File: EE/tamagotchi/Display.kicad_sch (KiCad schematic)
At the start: 0 parts

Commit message: Generic Continutation Checkin
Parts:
- added D1, D10, D11, D12, D2, D3, D4, D5, D6, D7, D8, D9: LED, symbol Device:LED
- added Q1, Q2, Q3, Q4: Q_NMOS_GDS, symbol Transistor_FET:Q_NMOS_GDS
- added R1, R10, R13, R14, R15, R16, R17, R18, R19, R2, R20, R7: R, symbol Device:R
- added R11, R3, R5, R8: 100k, symbol Device:R
- added R12, R4, R6, R9: 33, symbol Device:R
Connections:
- new net: Q3.1 (G), R9.2
- new net: D11.1 (K), D4.1 (K), Q3.2 (D)
- new net: D12.1 (K), D5.1 (K), Q4.2 (D)
- new net: D5.2 (A), R13.2
- new net: D11.2 (A), R19.2
- new net: D10.1 (K), D3.1 (K), Q2.2 (D)
- new net: D3.2 (A), R7.2
- new net: D1.1 (K), D2.1 (K), D6.1 (K), D7.1 (K), D8.1 (K), D9.1 (K), Q1.2 (D)
- new net: D6.2 (A), R14.2
- new net: D9.2 (A), R17.2
- new net: D4.2 (A), R10.2
- new net: D10.2 (A), R18.2
- new net: D12.2 (A), R20.2
- new net: Q4.1 (G), R12.2
- new net: D1.2 (A), R2.2
- new net: D2.2 (A), R1.2
- new net: Q1.1 (G), R4.2
- new net: Q2.1 (G), R6.2
- new net: D7.2 (A), R15.2
- new net: D8.2 (A), R16.2
- new net +3V3: R1.1, R10.1, R13.1, R14.1, R15.1, R16.1, R17.1, R18.1, R19.1, R2.1, R20.1, R7.1
- new net GND: Q1.3 (S), Q2.3 (S), Q3.3 (S), Q4.3 (S), R11.2, R3.2, R5.2, R8.2
- new net GREEN_EN: R11.1, R12.1
- new net RED_EN: R5.1, R6.1
- new net VAPE_EN: R3.1, R4.1
- new net YELLOW_EN: R8.1, R9.1
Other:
- note added: "Alcohol Backlight"
- note added: "Status Indicator"
- note added: "TODO screen"

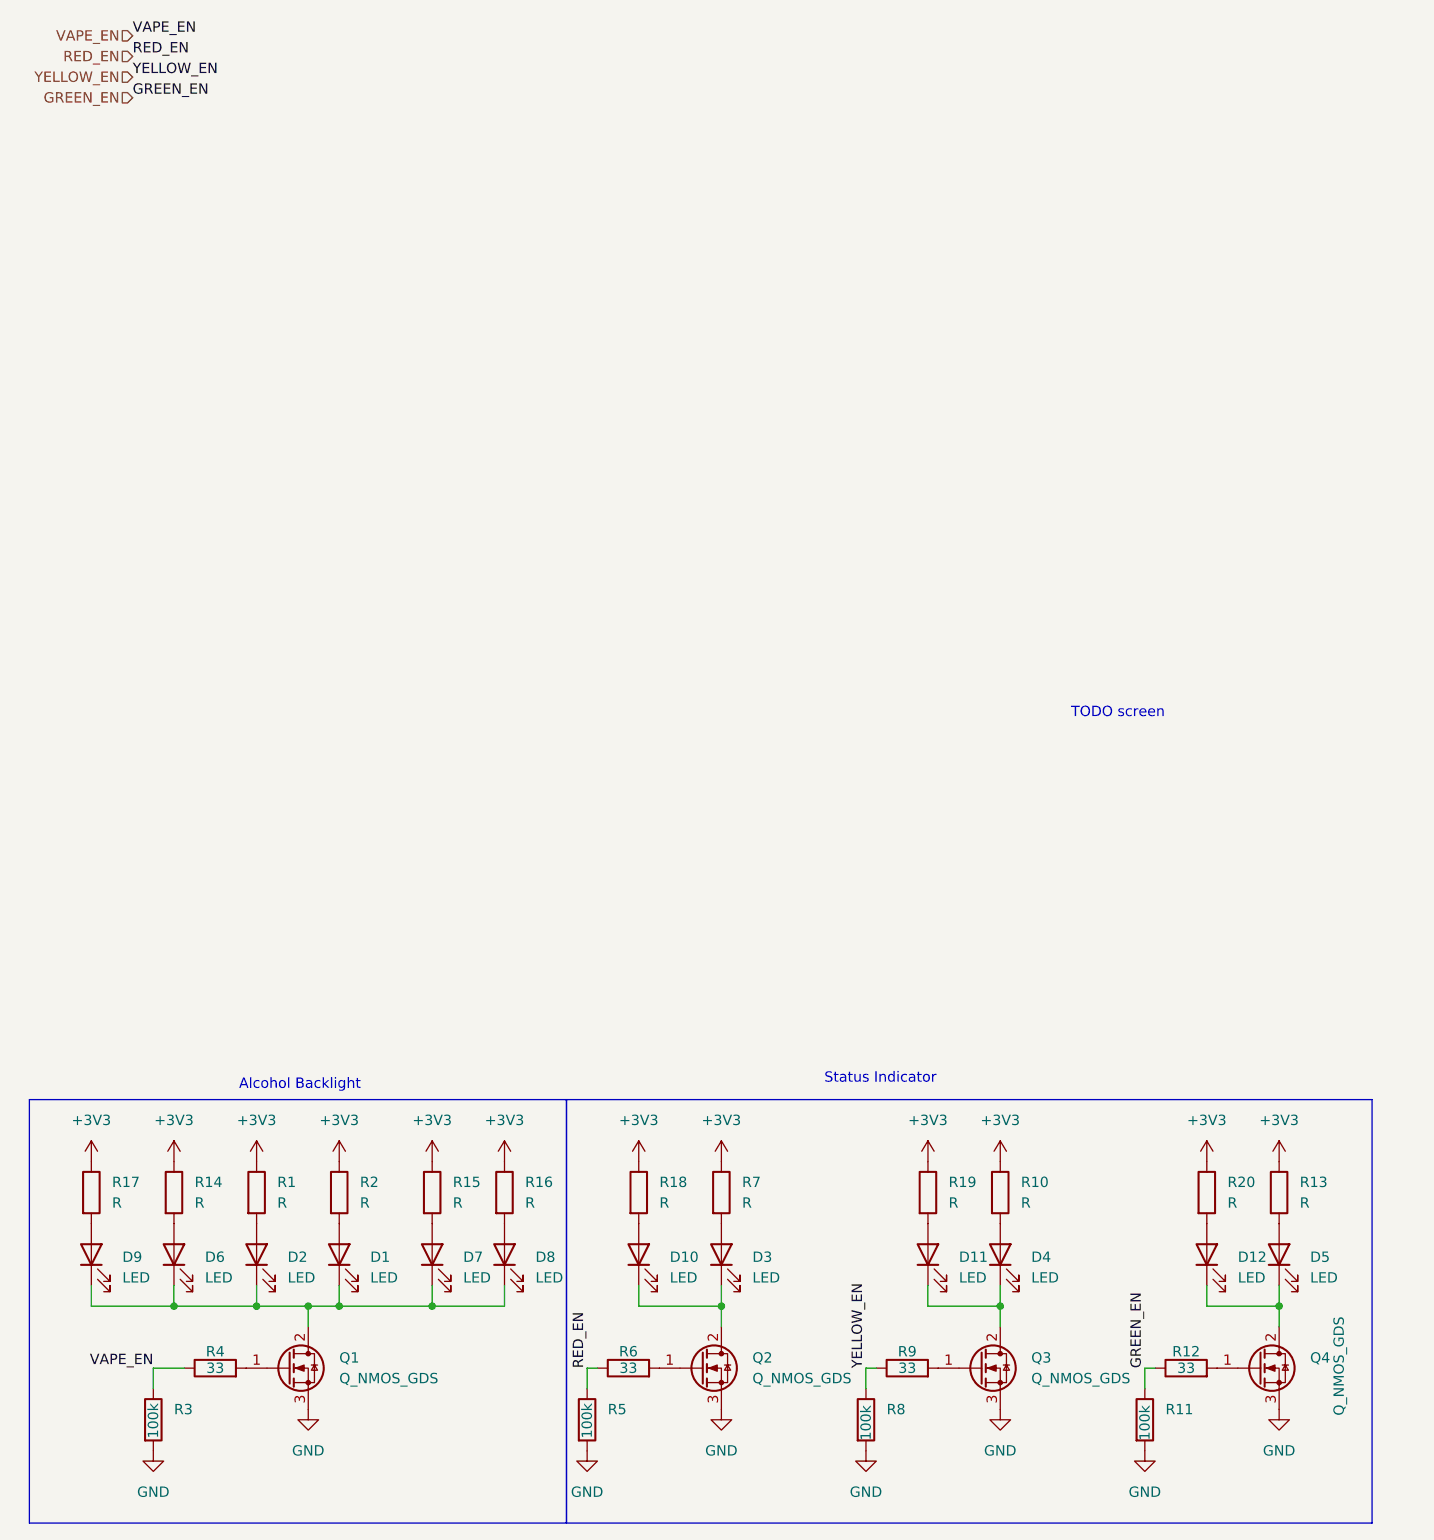
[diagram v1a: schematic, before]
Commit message: WIP - added 3D / footprints for devices. RGY LEDs aren't right
Need to do more outling / ect. super rough placement for everything.
LED footprint for RGY appears just wrong
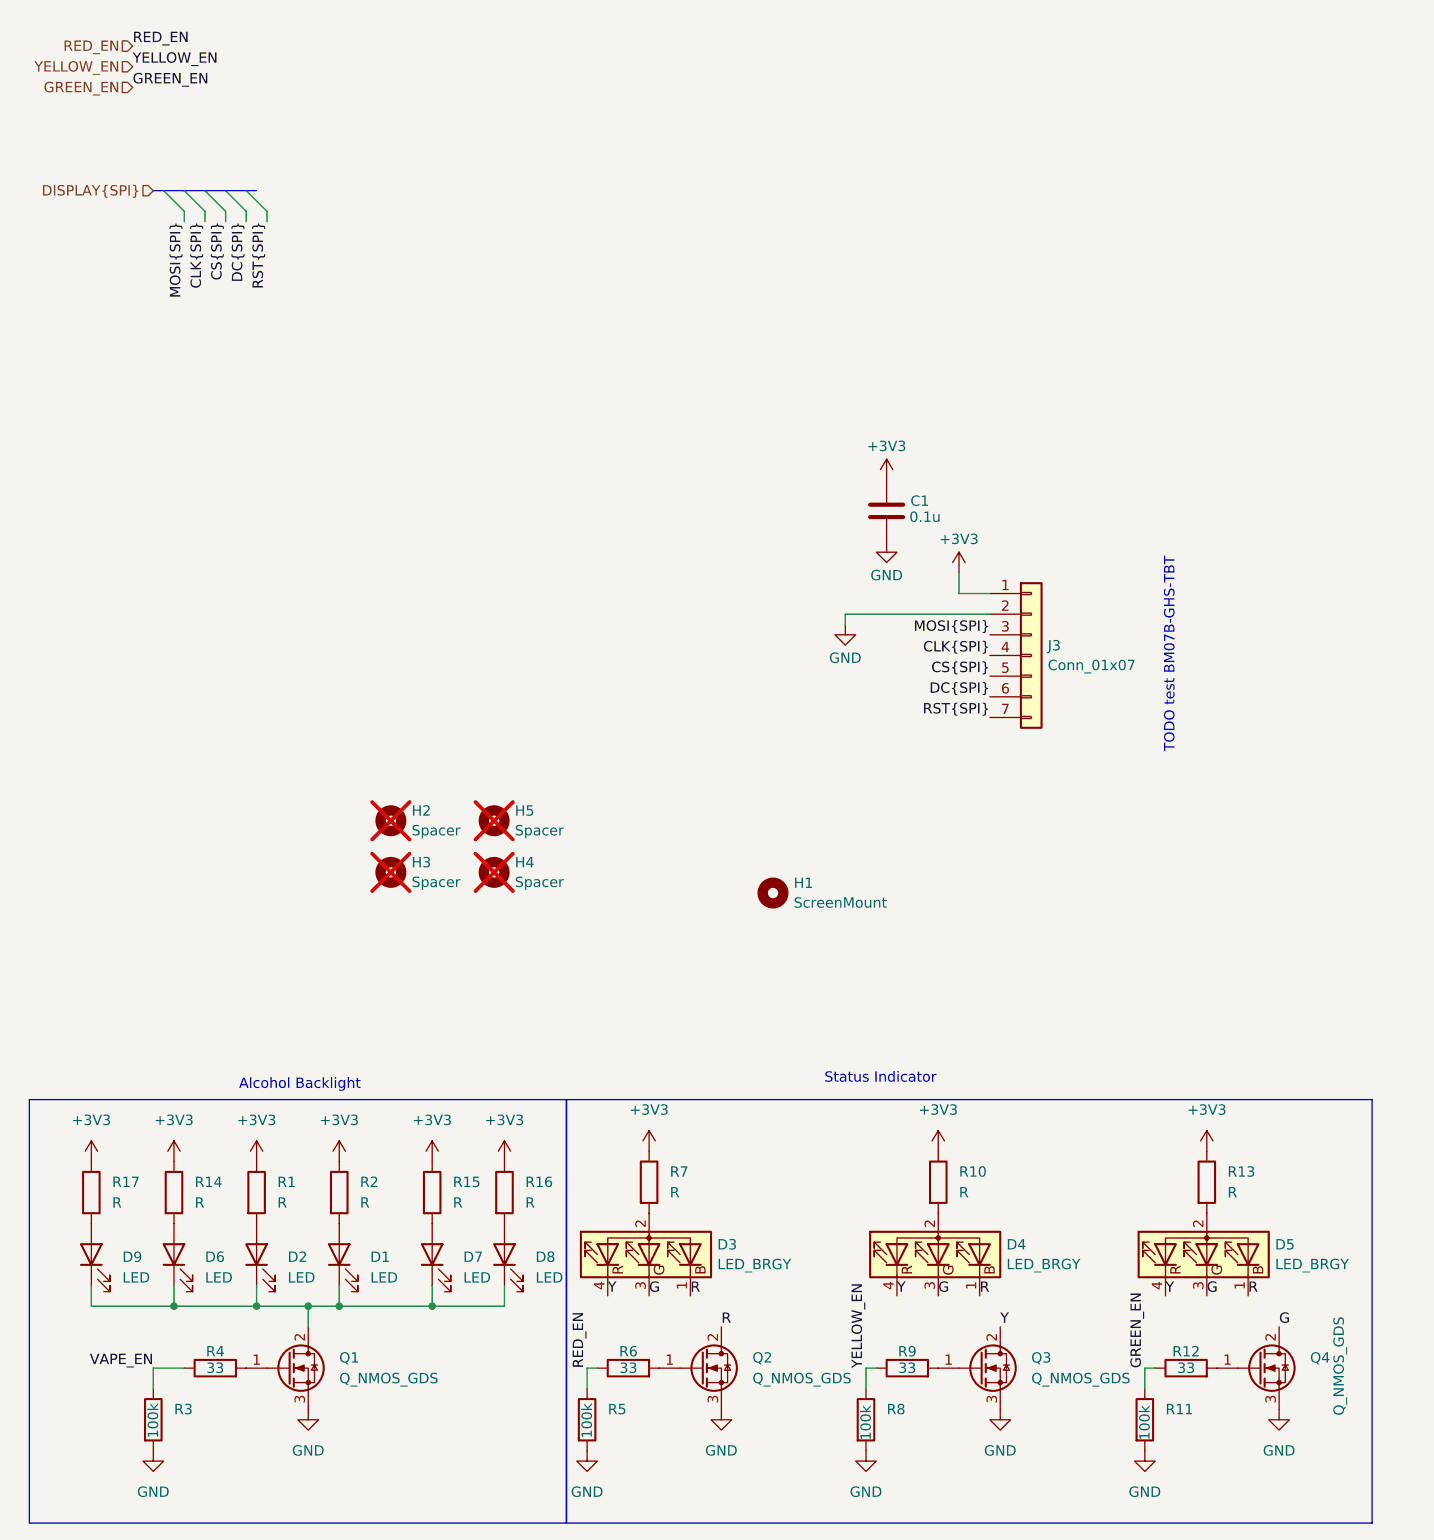
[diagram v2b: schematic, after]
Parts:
- removed D10, D11, D12, D3, D4, D5: LED, symbol Device:LED
- removed R18, R19, R20: R, symbol Device:R
- added C1: 0.1u, Capacitor_SMD:C_0402_1005Metric_Pad0.74x0.62mm_HandSolder, symbol Device:C
- added D3, D4, D5: LED_BRGY, Library:EAST1616RGYA0_EVE, symbol Device:LED_BAGR
- added H1: ScreenMount, Library:ScreenMount, symbol Mechanical:MountingHole
- added H2, H3, H4, H5: Spacer, symbol Mechanical:MountingHole
- added J3: Conn_01x07, symbol Connector_Generic:Conn_01x07
- D1, D2, D6, D7, D8, D9: footprint (none) -> LED_SMD:LED_0603_1608Metric_Pad1.05x0.95mm_HandSolder; MPN (none) -> 150060BS55040
- R1, R10, R11, R12, R13, R14, R15, R16, R17, R2, R3, R4, R5, R6, R7, R8, R9: footprint (none) -> Resistor_SMD:R_0402_1005Metric_Pad0.72x0.64mm_HandSolder
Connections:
- net +3V3: now also C1.1, J3.1 (Pin_1)
- net GND: now also C1.2, J3.2 (Pin_2)
- net Y: now reaches Q3.2 (D)
- net Y: now also D3.4 (RK), D4.4 (RK), D5.4 (RK)
- net G: now reaches Q4.2 (D)
- net G: now also D3.3 (GK), D4.3 (GK), D5.3 (GK)
- net at R13.2: now also D5.2 (A)
- net R: now reaches Q2.2 (D)
- net R: now also D3.1 (BK), D4.1 (BK), D5.1 (BK)
- net at R7.2: now also D3.2 (A)
- net at R10.2: now also D4.2 (A)
- new net CLK{SPI}: J3.4 (Pin_4)
- new net CS{SPI}: J3.5 (Pin_5)
- new net DC{SPI}: J3.6 (Pin_6)
- new net MOSI{SPI}: J3.3 (Pin_3)
- new net RST{SPI}: J3.7 (Pin_7)
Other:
- note added: "TODO test BM07B-GHS-TBT"
- note removed: "TODO screen"

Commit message: Footprints and mechanical parts assigned
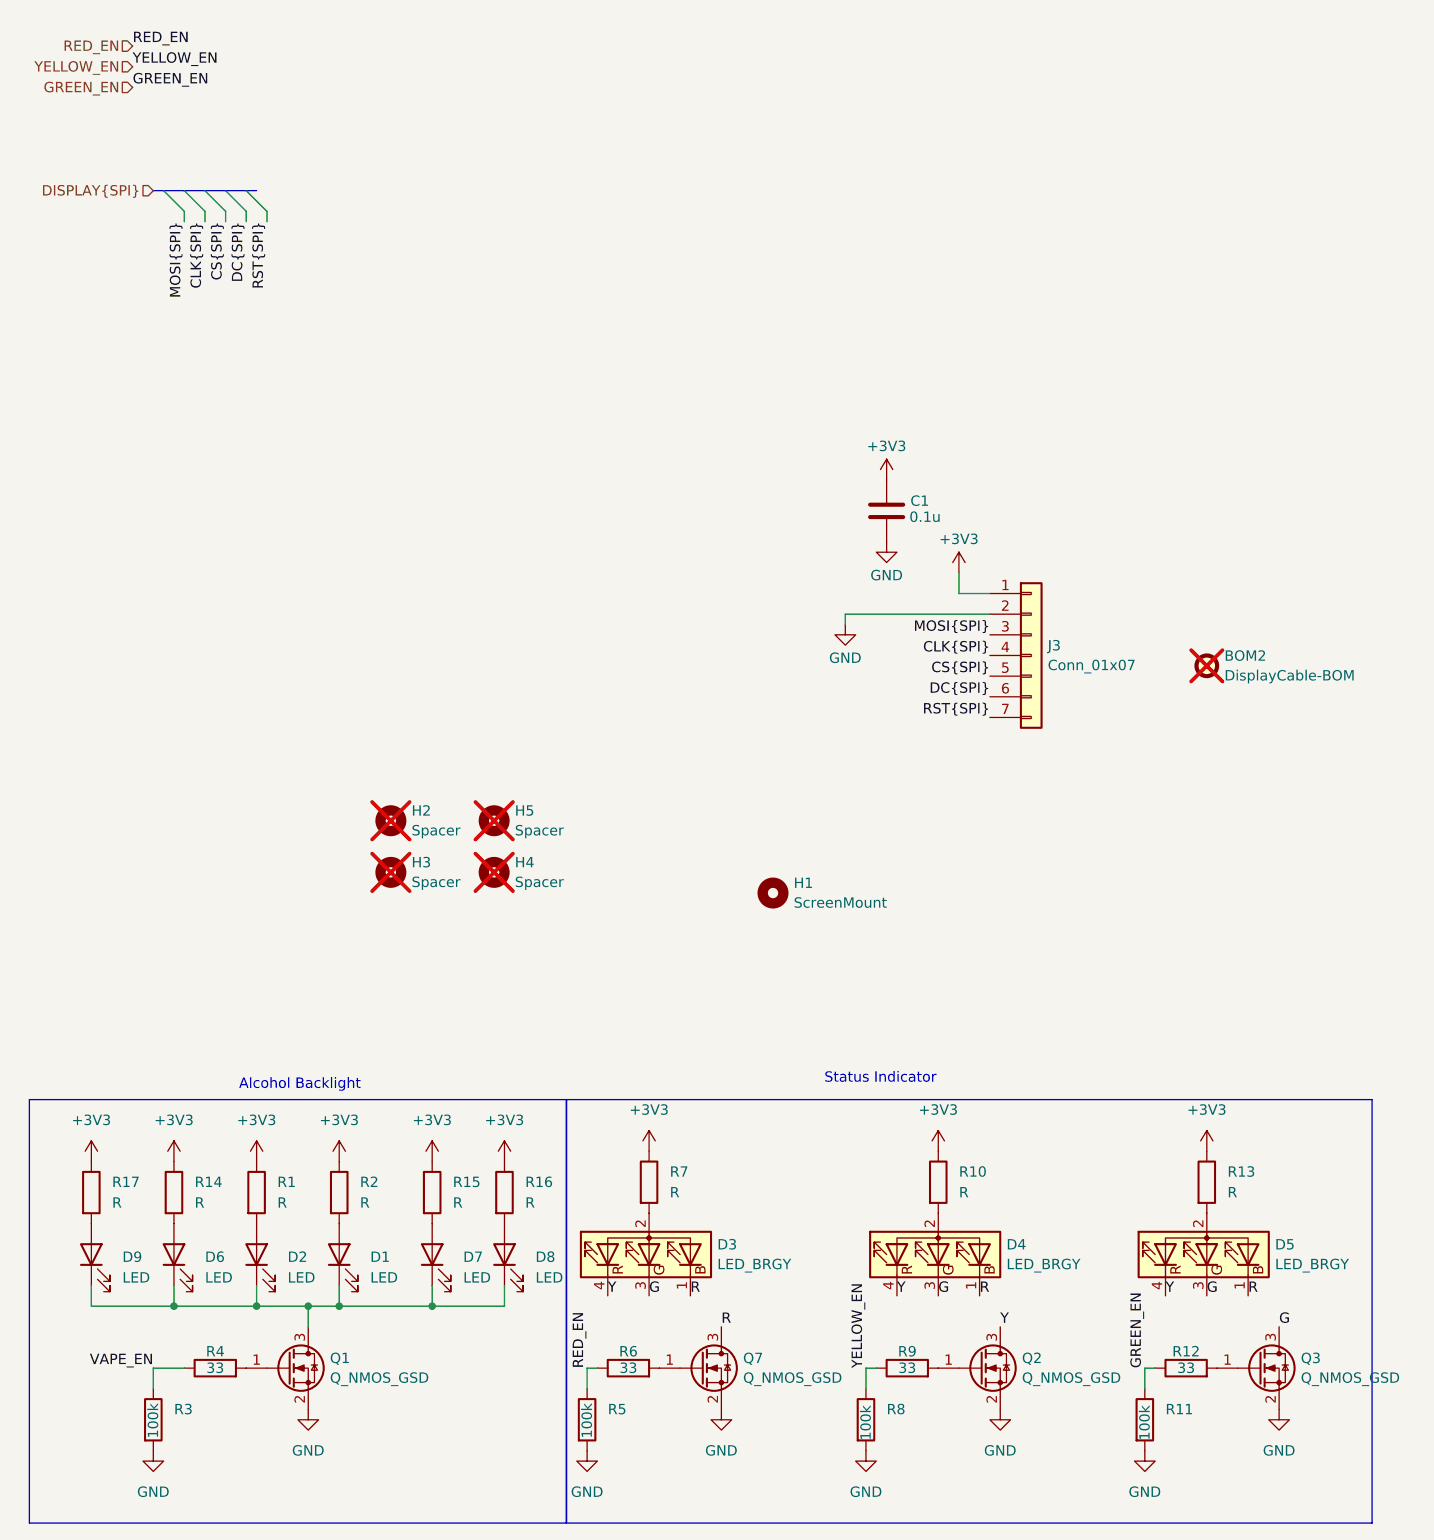
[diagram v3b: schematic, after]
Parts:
- removed Q1, Q2, Q3, Q4: Q_NMOS_GDS, symbol Transistor_FET:Q_NMOS_GDS
- added BOM2: DisplayCable-BOM, symbol Mechanical:Fiducial
- added Q1, Q2, Q3, Q7: Q_NMOS_GSD, Package_TO_SOT_SMD:SOT-23, symbol Transistor_FET:Q_NMOS_GSD
- J3: footprint (none) -> Library:MOLEX_532610771; MPN (none) -> 0532610771; TODO BM07B-GHS-TBT -> (none)
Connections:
- net G: now also Q3.3 (D)
- net GND: now also Q1.2 (S), Q2.2 (S), Q3.2 (S), Q7.2 (S)
- net R: now also Q7.3 (D)
- net Y: now also Q2.3 (D)
- net at R9.2: now also Q2.1 (G)
- net at D1.1 (K), D2.1 (K), D6.1 (K)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: now also Q1.3 (D)
- net at R12.2: now also Q3.1 (G)
- net at R4.2: now also Q1.1 (G)
- net at R6.2: now also Q7.1 (G)
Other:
- note removed: "TODO test BM07B-GHS-TBT"

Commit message: Migrated to 4 Layer. Added 3v3 and gnd layers
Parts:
- removed D2: LED, LED_SMD:LED_0603_1608Metric_Pad1.05x0.95mm_HandSolder, symbol Device:LED
- removed R1: R, Resistor_SMD:R_0402_1005Metric_Pad0.72x0.64mm_HandSolder, symbol Device:R
